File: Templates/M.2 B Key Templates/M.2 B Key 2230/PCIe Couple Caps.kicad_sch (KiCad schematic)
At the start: 2 parts

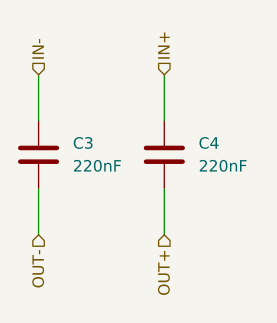
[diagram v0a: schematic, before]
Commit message: Added B Key Templates
-added B key Templates for all sizes
-corrected B key symbol pinout
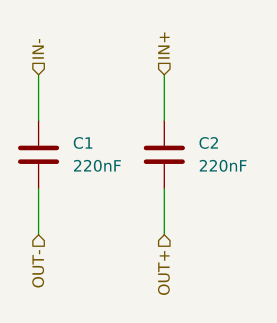
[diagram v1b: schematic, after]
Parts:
- renumbered C3 to C1, C4 to C2
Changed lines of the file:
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@@
 		(dnp no)
 		(fields_autoplaced yes)
-		(property "Reference" "C?"
+		(property "Reference" "C1"
 			(at 133.35 99.0599 0)
 			(effects
@@
 		)
 		(instances
-			(project "M.2 A Key 2230"
-				(path "/540e8a72-89ee-4807-aaa2-5d6c6cec308d/6a934661-433b-4364-b7d9-86a36dc44459/424c4cf5-3c3c-49ef-81c3-66eb0f823d39"
+			(project "M.2 B Key 2230"
+				(path "/e8aec58c-8555-41a0-bbe8-71a1cca0982a/6f3aec5e-6cbb-4c44-a88f-c2fbd765ff27/27d77bf0-8499-4672-87f1-05095c3d0a68"
 					(reference "C3")
 					(unit 1)
 				)
-				(path "/540e8a72-89ee-4807-aaa2-5d6c6cec308d/6a934661-433b-4364-b7d9-86a36dc44459/adcd4998-a306-4f2e-b87b-352712eb899b"
-					(reference "C2")
-					(unit 1)
-				)
-			)
-			(project "M.2 A Key"
-				(path "/d21209cf-d1f8-4eb7-aed8-e43843eefa7b/424c4cf5-3c3c-49ef-81c3-66eb0f823d39"
-					(reference "C?")
-					(unit 1)
-				)
-				(path "/d21209cf-d1f8-4eb7-aed8-e43843eefa7b/adcd4998-a306-4f2e-b87b-352712eb899b"
-					(reference "C?")
+				(path "/e8aec58c-8555-41a0-bbe8-71a1cca0982a/6f3aec5e-6cbb-4c44-a88f-c2fbd765ff27/2cd6dc77-f114-44b1-9704-d60d213c1d42"
+					(reference "C1")
 					(unit 1)
 				)
@@
 		(dnp no)
 		(fields_autoplaced yes)
-		(property "Reference" "C?"
+		(property "Reference" "C2"
 			(at 147.32 99.0599 0)
 			(effects
@@
 		)
 		(instances
-			(project "M.2 A Key 2230"
-				(path "/540e8a72-89ee-4807-aaa2-5d6c6cec308d/6a934661-433b-4364-b7d9-86a36dc44459/424c4cf5-3c3c-49ef-81c3-66eb0f823d39"
+			(project "M.2 B Key 2230"
+				(path "/e8aec58c-8555-41a0-bbe8-71a1cca0982a/6f3aec5e-6cbb-4c44-a88f-c2fbd765ff27/27d77bf0-8499-4672-87f1-05095c3d0a68"
 					(reference "C4")
 					(unit 1)
 				)
-				(path "/540e8a72-89ee-4807-aaa2-5d6c6cec308d/6a934661-433b-4364-b7d9-86a36dc44459/adcd4998-a306-4f2e-b87b-352712eb899b"
-					(reference "C1")
+				(path "/e8aec58c-8555-41a0-bbe8-71a1cca0982a/6f3aec5e-6cbb-4c44-a88f-c2fbd765ff27/2cd6dc77-f114-44b1-9704-d60d213c1d42"
+					(reference "C2")
 					(unit 1)
 				)
-			)
-			(project "M.2 A Key"
-				(path "/d21209cf-d1f8-4eb7-aed8-e43843eefa7b/424c4cf5-3c3c-49ef-81c3-66eb0f823d39"
-					(reference "C?")
-					(unit 1)
-				)
-				(path "/d21209cf-d1f8-4eb7-aed8-e43843eefa7b/adcd4998-a306-4f2e-b87b-352712eb899b"
-					(reference "C?")
-					(unit 1)
-				)
